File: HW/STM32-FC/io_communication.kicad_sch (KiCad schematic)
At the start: 12 parts, among them J11 TELE1, J12 TELE2, J13 I2C, J14 CAN, U10 ATA6561-GAQW

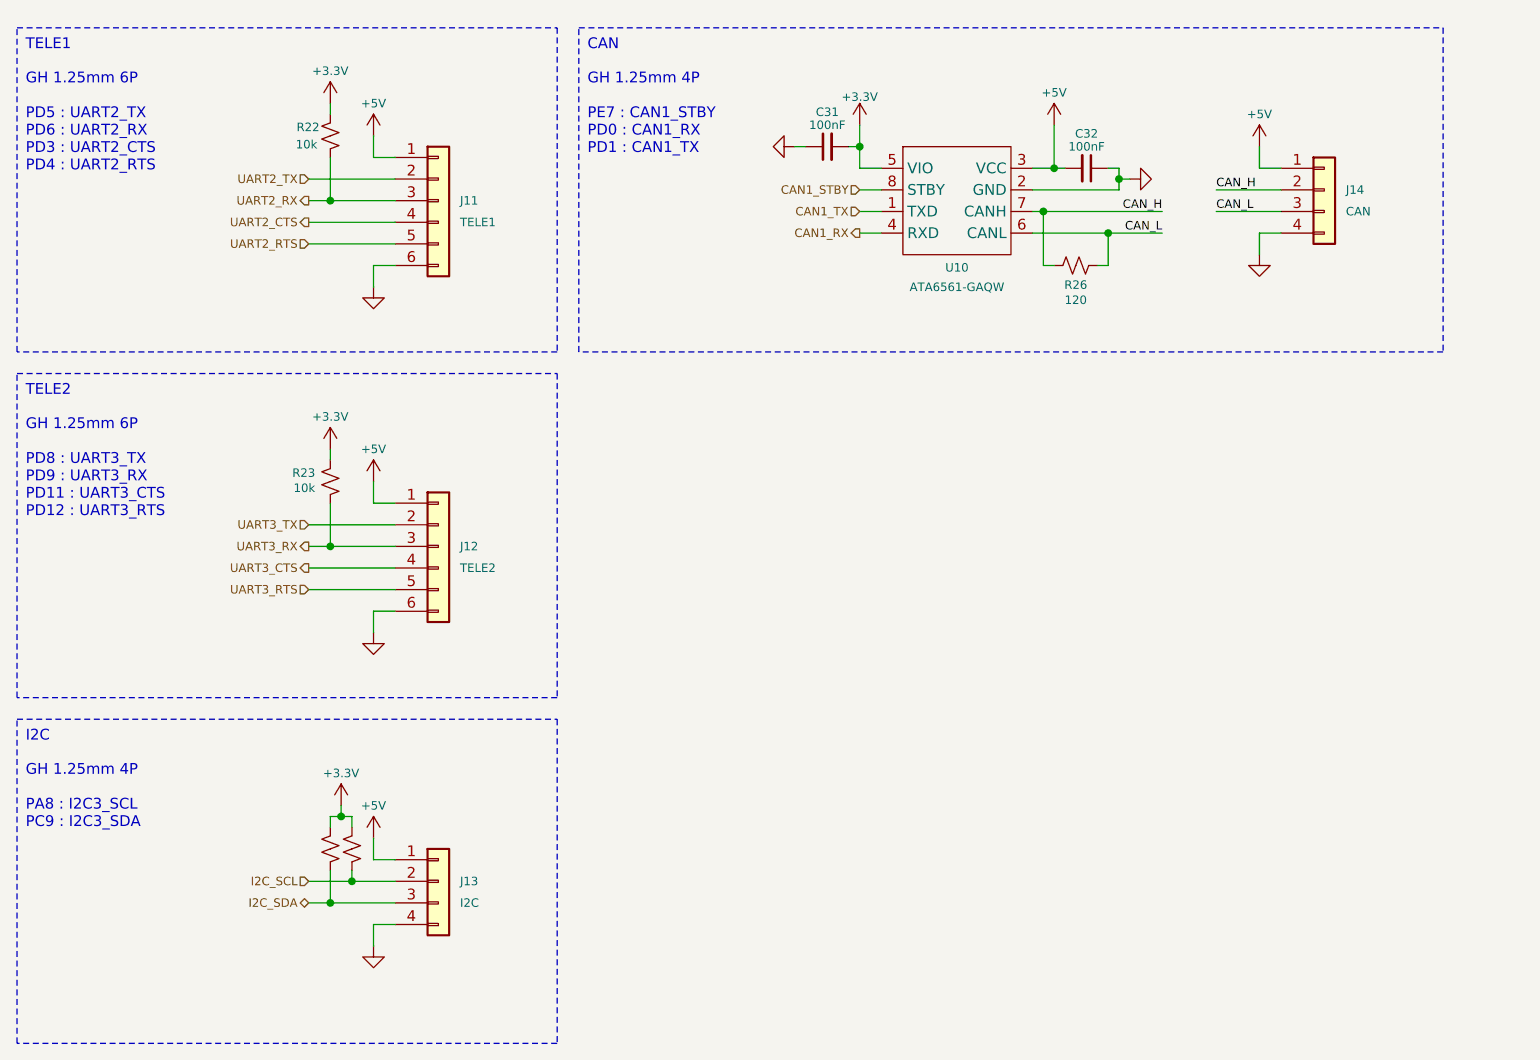
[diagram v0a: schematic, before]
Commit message: 2025.01.03v2:PM(Power Module) added
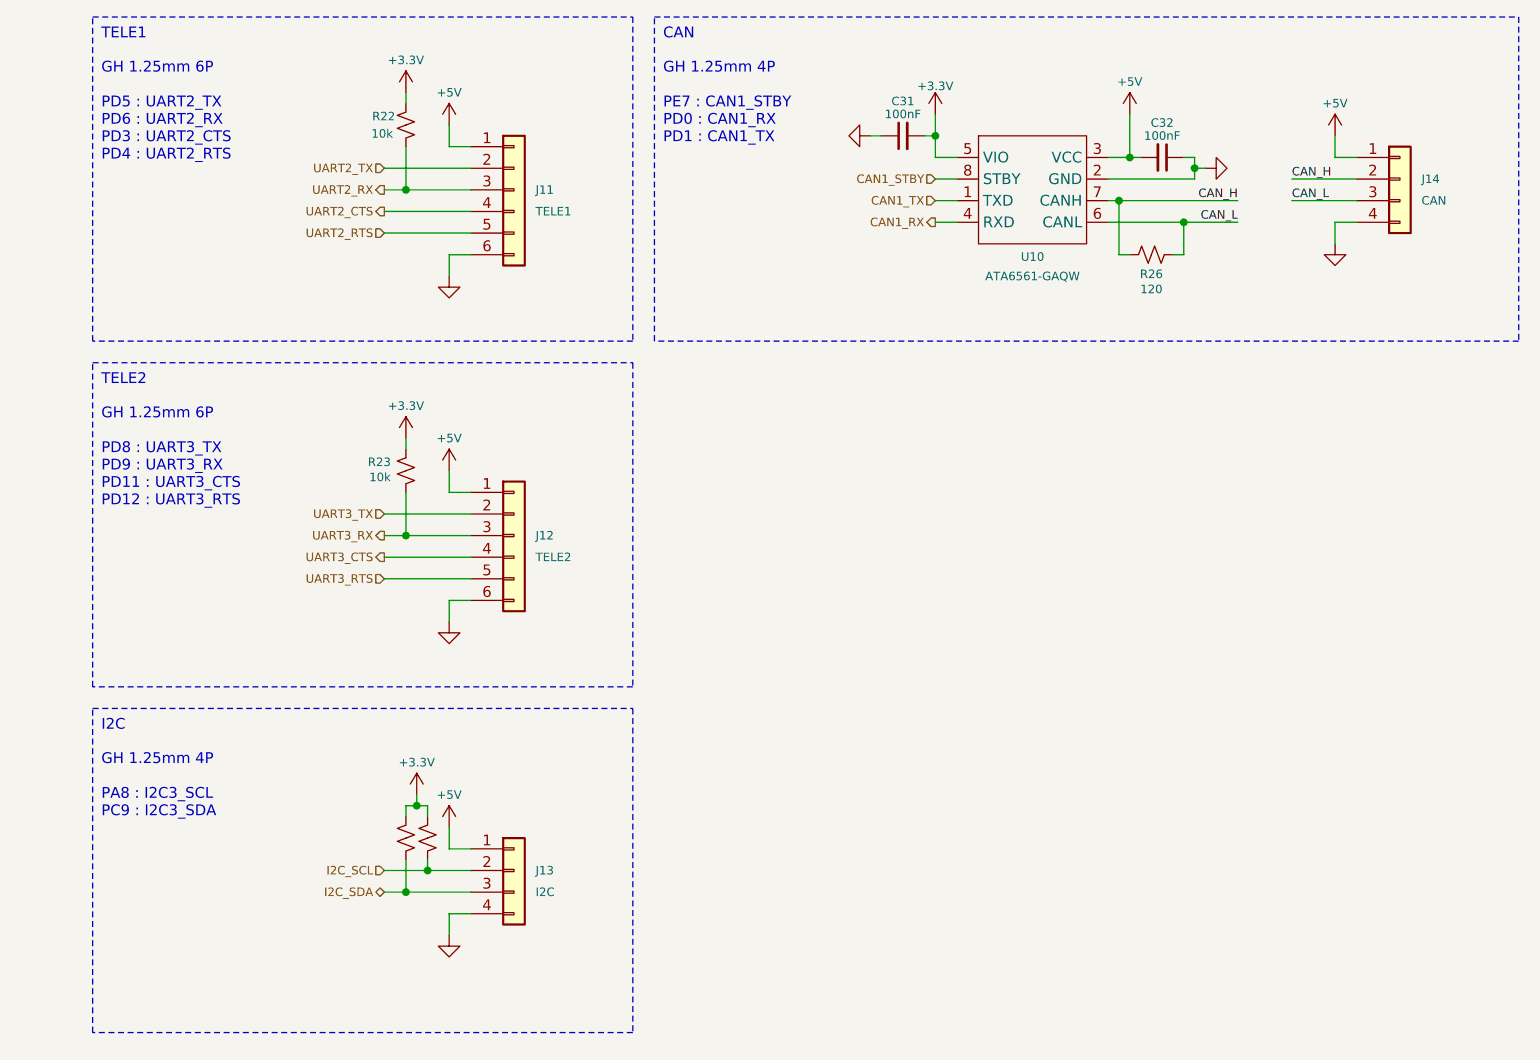
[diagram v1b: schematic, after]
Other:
- company: INHA UNIV. NARAE -> NARAE
- moved on the sheet: C31, C32, J11, J12, J13, J14, R22, R23, R26, U10

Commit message: Baro/SD Card update
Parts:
- added C32, C34: 100nF, Capacitor_SMD:C_0402_1005Metric, symbol Device:C_Small
- added J18: GH 1.25mm 4P, JST_GH:JST_GH_BM04B-GHS-TBT_04, symbol Connector_Generic:Conn_01x04
- added R33: 120, Resistor_SMD:R_0402_1005Metric, symbol Device:R_Small_US
- added U11: ATA6561-GBQW, ATA6561:VDFN8_3X3_MCH_HandSolder, symbol ATA6561-GBQW:ATA6561-GBQW_2
- J14: renamed from J11; value TELE1 -> GH 1.25mm 6P; footprint Connectors_JST:JST_GH_BM06B-GHS-TBT_06x1.25mm_Straight -> JST_GH:JST_GH_BM06B-GHS-TBT_06
- J15: renamed from J12; value TELE2 -> GH 1.25mm 6P; footprint Connectors_JST:JST_GH_BM06B-GHS-TBT_06x1.25mm_Straight -> JST_GH:JST_GH_BM06B-GHS-TBT_06
- J16: renamed from J13; value I2C -> GH 1.25mm 4P; footprint Connectors_JST:JST_GH_BM04B-GHS-TBT_04x1.25mm_Straight -> JST_GH:JST_GH_BM04B-GHS-TBT_04
- J17: renamed from J14; value CAN -> GH 1.25mm 4P; footprint Connectors_JST:JST_GH_BM04B-GHS-TBT_04x1.25mm_Straight -> JST_GH:JST_GH_BM04B-GHS-TBT_04
- U10: value ATA6561-GAQW -> ATA6561-GBQW; footprint Package_SO:SOIC-8_3.9x4.9mm_P1.27mm -> ATA6561:VDFN8_3X3_MCH_HandSolder; symbol ATA6561-GAQW:ATA6561-GAQW_2 -> ATA6561-GBQW:ATA6561-GBQW_2
- renumbered C32 to C33, R22 to R28, R23 to R29, R24 to R30, R25 to R31, R26 to R32
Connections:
- net +3.3V: now also C32.2, U11.5 (VIO)
- net +5V: now also C34.2, J18.1 (Pin_1), U11.3 (VCC)
- net GND: now also U10.9 (EPAD), C32.1, C34.1, J18.4 (Pin_4), U11.2 (GND), U11.9 (EPAD)
- net CAN_H renamed CAN1_H
- net CAN_L renamed CAN1_L
- new net CAN2_H: J18.2 (Pin_2), R33.1, U11.7 (CANH)
- new net CAN2_L: J18.3 (Pin_3), R33.2, U11.6 (CANL)
- new net CAN2_RX: U11.4 (RXD)
- new net CAN2_STBY: U11.8 (STBY)
- new net CAN2_TX: U11.1 (TXD)
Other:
- note added: "CAN1"
- note added: "CAN2"
- note added: "GH 1.25mm 4P PC4 : CAN1_STBY PD0 : CAN1_RX PD1 : CAN1_TX"
- note added: "GH 1.25mm 4P PC5 : CAN2_STBY PB6 : CAN2_RX PB12 : CAN2_TX"
- note removed: "CAN"
- note removed: "GH 1.25mm 4P PE7 : CAN1_STBY PD0 : CAN1_RX PD1 : CAN1_TX"
- moved on the sheet: C33, J14, J15, J16, J17, R28, R29, R32

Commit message: 2025.01.16
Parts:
- renumbered C33 to C32, C32 to C33, J17 to J14, J14 to J15, J18 to J16, J15 to J17, J16 to J18, R32 to R29, R29 to R30, R33 to R31, R30 to R32, R31 to R33

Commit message: 2025.01.17 : PCB layout
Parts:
- U10, U11: footprint ATA6561:VDFN8_3X3_MCH_HandSolder -> ATA6561:VDFN8_3X3_MCH-L
- renumbered C33 to C32, C32 to C33, J15 to J11, J17 to J12, J18 to J13, J16 to J15, R28 to R29, R32 to R31, R33 to R32, R29 to R33, R31 to R34

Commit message: 2025.01.17 Differential Pair update
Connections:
- net CAN1_H renamed CAN1_P
- net CAN1_L renamed CAN1_N
- net CAN2_H renamed CAN2_P
- net CAN2_L renamed CAN2_N
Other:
- moved on the sheet: J14, J15

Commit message: 2025.02.06 PCB routing done v2
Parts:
- C31, C32, C33, C34: LCSC C1525 -> C1581
- J11, J12: LCSC (none) -> C189892
- J13, J14, J15: LCSC (none) -> C161692
- R29, R30, R31, R32: LCSC (none) -> C25531
- R33, R34: LCSC (none) -> C25079
- U10, U11: LCSC (none) -> C617297
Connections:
- net +5V: now also J11.6 (Pin_6), J12.6 (Pin_6), J13.4 (Pin_4), J14.4 (Pin_4), J15.4 (Pin_4); no longer J11.1 (Pin_1), J12.1 (Pin_1), J13.1 (Pin_1), J14.1 (Pin_1), J15.1 (Pin_1)
- net CAN1_N: now also J14.2 (Pin_2); no longer J14.3 (Pin_3)
- net CAN1_P: now also J14.3 (Pin_3); no longer J14.2 (Pin_2)
- net CAN2_N: now also J15.2 (Pin_2); no longer J15.3 (Pin_3)
- net CAN2_P: now also J15.3 (Pin_3); no longer J15.2 (Pin_2)
- net GND: now also J11.1 (Pin_1), J12.1 (Pin_1), J13.1 (Pin_1), J14.1 (Pin_1), J15.1 (Pin_1); no longer J11.6 (Pin_6), J12.6 (Pin_6), J13.4 (Pin_4), J14.4 (Pin_4), J15.4 (Pin_4)
- net I2C_SCL: now also J13.3 (Pin_3); no longer J13.2 (Pin_2)
- net I2C_SDA: now also J13.2 (Pin_2); no longer J13.3 (Pin_3)
- net UART2_CTS: now also J11.3 (Pin_3); no longer J11.4 (Pin_4)
- net UART2_RTS: now also J11.2 (Pin_2); no longer J11.5 (Pin_5)
- net UART2_RX: now also J11.4 (Pin_4); no longer J11.3 (Pin_3)
- net UART2_TX: now also J11.5 (Pin_5); no longer J11.2 (Pin_2)
- net UART3_CTS: now also J12.3 (Pin_3); no longer J12.4 (Pin_4)
- net UART3_RTS: now also J12.2 (Pin_2); no longer J12.5 (Pin_5)
- net UART3_RX: now also J12.4 (Pin_4); no longer J12.3 (Pin_3)
- net UART3_TX: now also J12.5 (Pin_5); no longer J12.2 (Pin_2)
